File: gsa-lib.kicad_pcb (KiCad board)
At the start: 2 copper layers, 91 parts

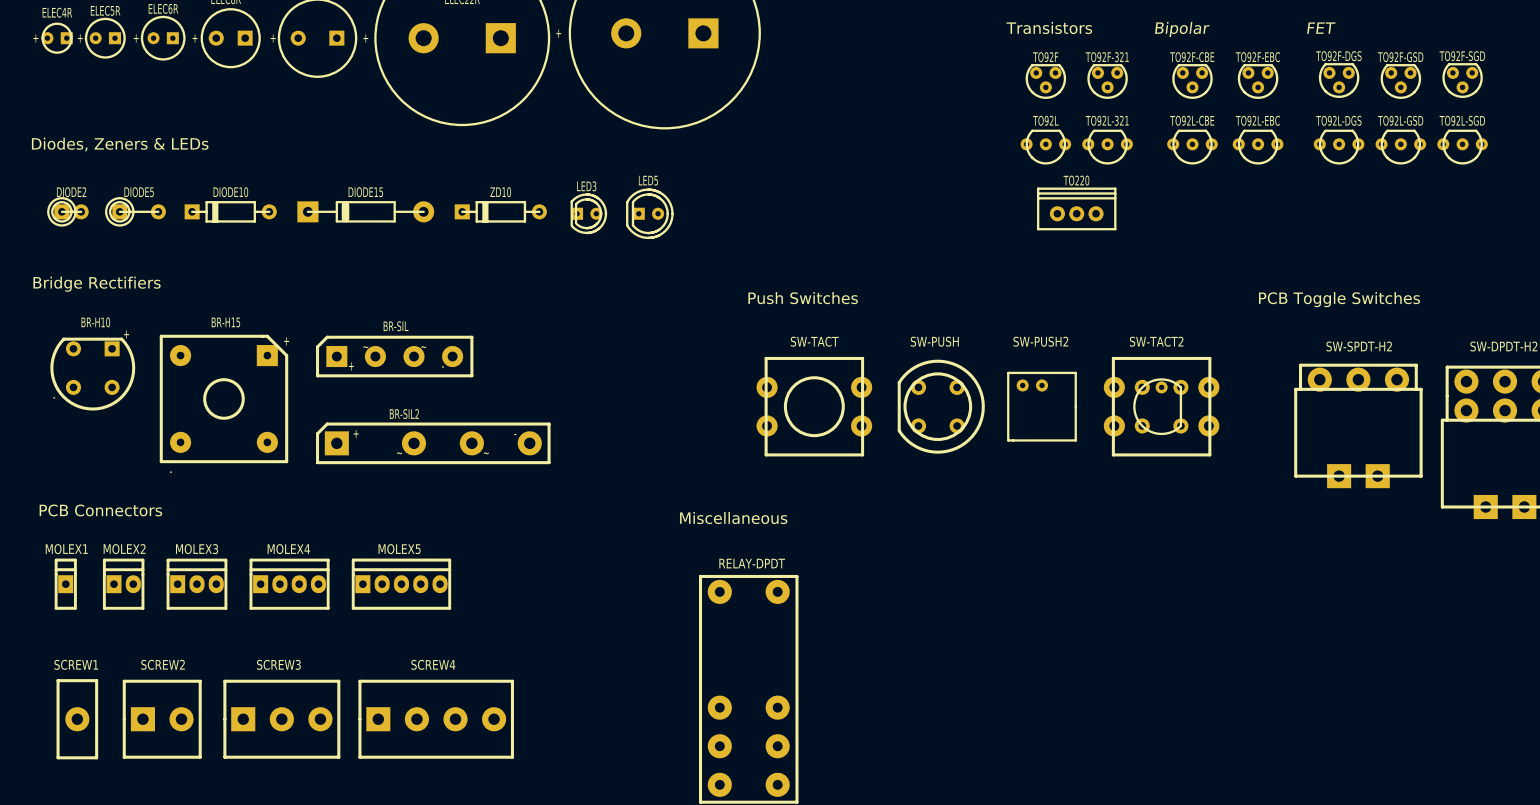
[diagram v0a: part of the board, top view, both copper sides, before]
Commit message: Add green LED variants to 3D models
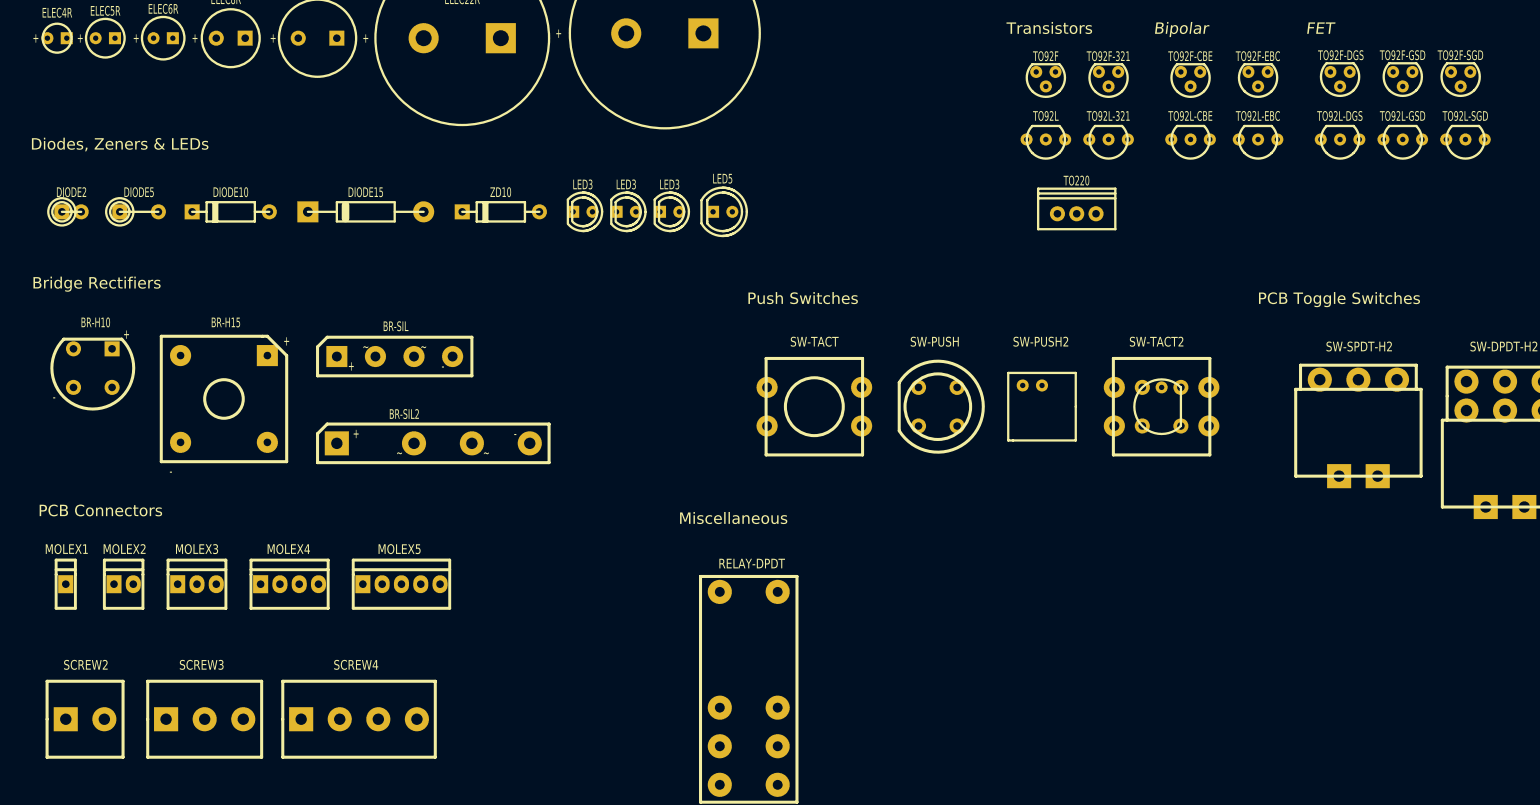
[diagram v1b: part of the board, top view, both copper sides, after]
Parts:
- removed SCREW1: 1term, gsa:SCREW1
- added LED3: 3mm, gsa:LED3, F.Cu at (102.9, 105.4)
- added LED3: 3mm, gsa:LED3, F.Cu at (97.2, 105.4)
- PAD-L: footprint gsa:PAD-XL -> gsa:PAD-L
- PAD-M: footprint gsa:PAD-L -> gsa:PAD-M
- PAD-S: footprint gsa:PAD-M -> gsa:PAD-S
- PAD-T: footprint gsa:PAD-S -> gsa:PAD-T
- PAD-XL: footprint gsa:PAD-XXL -> gsa:PAD-XL
- moved SCREW3 10.2 mm to (41.7, 172.2)
- moved SCREW2 10.2 mm to (25.9, 172.2)
- moved SCREW4 10.2 mm to (62.0, 172.2)
- moved LED5 9.78 mm to (109.9, 105.4)
- moved TO92L-SGD 0.74 mm to (207.6, 95.9)
- moved TO92L-CBE 0.68 mm to (171.4, 95.9)
- moved TO92L-GSD 0.68 mm to (199.4, 95.9)
- moved TO92L-321 0.65 mm to (160.7, 95.9)
- moved TO92L-DGS 0.65 mm to (191.1, 95.9)
- moved TO92L 0.63 mm to (152.4, 95.9)
- moved TO92L-EBC 0.63 mm to (180.3, 95.9)
- moved LED3 0.57 mm to (91.4, 105.4)
- moved TO92F-CBE 0.28 mm to (171.4, 88.3)
- moved TO92F-SGD 0.28 mm to (207.0, 88.3)
- moved TO92F-GSD 0.28 mm to (199.4, 88.3)
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
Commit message: Symbol and Footprint updates for GSA Emerald II
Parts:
- removed PAD-T: 0.7mm, gsa:PAD-T
- added LOGO-S: , gsa:LOGO-S, F.Cu at (140.5, 190.0)
- added LOGO_L: , gsa:LOGO-L, F.Cu at (125.5, 186.7)
- added LOGO_XS: , gsa:LOGO-XS, F.Cu at (140.5, 177.0)
- added PAD-XS: 0.7mm, gsa:PAD-XS, F.Cu at (19.1, 31.8)
- added POT-SNAP-H: , gsa:POT-SNAP-H, F.Cu at (245.1, 25.4)
- added POT-SNAP-V: , gsa:POT-SNAP-V, F.Cu at (260.4, 25.4)
- added POT-TRIM-H: , gsa:POT-TRIM-H, F.Cu at (245.1, 109.2)
- added SOIC8: 8pin SOIC, gsa:SOIC8, F.Cu at (180.3, 53.3)
- added SOT23-BCE: , gsa:SOT23-BCE, F.Cu at (171.4, 104.8)
- added SOT23-DGS: , gsa:SOT23-DGS, F.Cu at (191.1, 104.8)
- added TO92F-DSG: , gsa:TO92F-DSG, F.Cu at (215.3, 88.3)
- added TO92L-DSG: , gsa:TO92L-DSG, F.Cu at (215.9, 95.9)
- added TRIM-L: , gsa:TRIM-L, F.Cu at (238.8, 70.5)
- added TRIM-VS: , gsa:TRIM-VS, F.Cu at (238.8, 95.2)
- LED3: value 3mm -> 2mm
- moved TRIM-HS 40.4 mm to (238.8, 85.1)
- moved TRIM-V 24.0 mm to (238.8, 61.0)
- moved RELAY-DPDT 23.5 mm to (89.9, 153.4)
- moved TRIM-H 9.89 mm to (238.8, 48.3)
- moved POT-16 1.80 mm to (260.4, 70.4)
- moved POT-16-D 1.80 mm to (261.9, 90.7)
- moved POT-OMEG 1.80 mm to (256.3, 111.5)
- moved POT-DUAL 1.80 mm to (263.9, 152.7)
- moved POT-MIN 1.80 mm to (255.8, 39.4)
- moved POT-MIN-D 1.80 mm to (258.3, 53.1)
- moved POT-OMEG-D 1.80 mm to (263.9, 131.8)

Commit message: Overhaul and tidy-up of symbols, footprints and 3D models
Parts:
- removed 15pin TO220: TO220-15, gsa:TO220-15
- removed BR-SIL2: , gsa:BR-SIL2
- removed CAP-5-7: 5/7.5mm leads, gsa:CAP-5-7
- removed CAP-5-7-10: 5/7.5/10mm leads, gsa:CAP-5-7-10
- removed CAP1350: 13x5mm, gsa:CAP1350
- removed DIODE5: 5mm, gsa:DIODE5
- removed ELEC22R: 22mm, gsa:ELEC22R
- removed HOLE33: 3.3mm, gsa:HOLE33
- removed LOGO-S: , gsa:LOGO-S
- removed MOLEX5: 5pin, gsa:MOLEX5
- removed PAD-L: 1.5mm, gsa:PAD-L
- removed PAD-M: 1.3mm, gsa:PAD-M
- removed PAD-S: 1mm, gsa:PAD-S
- removed PAD-XL: 2.1mm, gsa:PAD-XL
- removed PAD-XS: 0.7mm, gsa:PAD-XS
- removed POT-DUAL: , gsa:POT-DUAL
- removed POT-TRIM-H: , gsa:POT-TRIM-H
- removed RELAY-DPDT: , gsa:RELAY-DPDT
- removed RES12: 12mm, gsa:RES12
- removed RES15: 15mm, gsa:RES15
- removed RES2: 2.5mm, gsa:RES2
- removed RES20: 20mm, gsa:RES20
- removed SCREW3: 3term, gsa:SCREW3
- removed SOT23-BCE: , gsa:SOT23-BCE
- removed SOT23-DGS: , gsa:SOT23-DGS
- removed SW-PUSH: , gsa:SW-PUSH
- removed SW-TACT2: , gsa:SW-TACT2
- removed TO92F-321: , gsa:TO92F-321
- removed TO92F-SGD: , gsa:TO92F-SGD
- removed TO92L-321: , gsa:TO92L-321
- removed TO92L-SGD: , gsa:TO92L-SGD
- removed ZD10: 10mm, gsa:ZENER10
- added 0.7mm: PAD07, gsa:PAD07, F.Cu at (19.1, 31.1)
- added 1.0mm: PAD10, gsa:PAD10, F.Cu at (24.8, 31.1)
- added 1.3mm: PAD13, gsa:PAD13, F.Cu at (31.1, 31.8)
- added 1.5mm: PAD15, gsa:PAD15, F.Cu at (37.5, 31.8)
- added 10mm: DIODE10, gsa:DIODE10, F.Cu at (44.5, 99.7)
- added 10x7mm: CAP1070, gsa:CAP1070, F.Cu at (104.1, 63.5)
- added 12.5mm: RES12, gsa:RES12, F.Cu at (66.0, 45.7)
- added 15mm: RES15, gsa:RES15, F.Cu at (83.8, 45.7)
- added 2.1mm: PAD21, gsa:PAD21, F.Cu at (44.5, 31.8)
- added 2.5mm: DIODE2, gsa:DIODE2, F.Cu at (23.5, 99.7)
- added 2.5mm: RES2, gsa:RES2, F.Cu at (19.7, 45.7)
- added 20mm: RES20, gsa:RES20, F.Cu at (105.4, 45.7)
- added 22mm: ELEC22R, gsa:ELEC22R, F.Cu at (75.6, 84.5)
- added 3.3mm: HOLE33-G, gsa:HOLE33-G, F.Cu at (59.7, 32.4)
- added 3.3mm: HOLE33, gsa:HOLE33, F.Cu at (51.4, 31.8)
- added 3term: SCREW3, gsa:SCREW3, F.Cu at (41.0, 174.8)
- added 5mm: DIODE5, gsa:DIODE5, F.Cu at (32.4, 99.7)
- added 5mm: RECT5, gsa:DIODE5, F.Cu at (33.0, 110.5)
- added 5pin: MOLEX5, gsa:MOLEX5, F.Cu at (66.9, 157.0)
- added 7.5/10mm: CAP-7-10, gsa:CAP-7-10, F.Cu at (116.8, 63.5)
- added 8mm: RES8, gsa:RES8, F.Cu at (38.1, 45.7)
- added ?: SOT23-DSG, gsa:SOT23-DSG, F.Cu at (199.4, 106.7)
- added ?: SOT23-GSD, gsa:SOT23-GSD, F.Cu at (209.6, 106.7)
- added ?: BR-SIL2, gsa:BR-SIL2, F.Cu at (68.0, 127.0)
- added ?: SW-PUSH1, gsa:SW-PUSH1, F.Cu at (191.1, 132.1)
- added ?: TO220-15, gsa:TO220-15, F.Cu at (179.1, 31.1)
- added ?: TO92L-ECB, gsa:TO92L-ECB, F.Cu at (188.0, 98.4)
- added ?: SW-DPDT-V2, gsa:SW-DPDT-V2, F.Cu at (168.3, 135.9)
- added ?: TO92F-ECB, gsa:TO92F-ECB, F.Cu at (188.0, 90.8)
- added ?: RELAY-DPDT, gsa:RELAY-DPDT, F.Cu at (88.3, 181.6)
- added ?: SOT23-BEC, gsa:SOT23-BEC, F.Cu at (167.6, 106.7)
- added ?: SOT23, gsa:SOT23, F.Cu at (153.0, 106.7)
- added ?: TO220-5, gsa:TO220-5, F.Cu at (198.8, 31.1)
- added ?: LOGO_S, gsa:LOGO-S, F.Cu at (140.3, 189.9)
- added ?: TO220-11, gsa:TO220-11, F.Cu at (156.2, 31.1)
- added Combined Pots: POT-DUAL, gsa:POT-DUAL, F.Cu at (265.4, 158.1)
- added Combined Push Switches: SW-TACT-ALL, gsa:SW-TACT-ALL, F.Cu at (210.2, 149.2)
- added Reversible Pot/Trimmer: POT-TRIM-HR, gsa:POT-TRIM-HR, F.Cu at (247.0, 115.6)
- 10mm: renamed from ELEC10R; value 10mm -> ELEC10R
- 10mm: renamed from DIODE10; value 10mm -> RECT10
- 10mm: renamed from RES10; value 10mm -> RES10
- 10x3.5mm: renamed from CAP1035; value 10x3.5mm -> CAP1035
- 14pin DIL: renamed from DIL14; value 14pin DIL -> DIL14
- 15mm: renamed from DIODE15; value 15mm -> RECT15
- 16pin DIL: renamed from DIL16; value 16pin DIL -> DIL16
- 1pin: renamed from MOLEX1; value 1pin -> MOLEX1
- 2.5mm: renamed from DIODE2; value 2.5mm -> RECT2
- 2.5mm: renamed from LINK2; value 2.5mm -> LINK2
- 2.5mm: renamed from CAP-C25; value 2.5mm -> CAP-C25
- 25mm: renamed from ELEC25R; value 25mm -> ELEC25R
- 2mm: renamed from LED3; value 2mm -> LED3
- 2pin: renamed from MOLEX2; value 2pin -> MOLEX2
- 2term: renamed from SCREW2; value 2term -> SCREW2
- 3mm (x2): renamed from LED3; value 3mm -> LED3
- 3pin: renamed from MOLEX3; value 3pin -> MOLEX3
- 4mm: renamed from ELEC4R; value 4mm -> ELEC4R
- 4pin: renamed from MOLEX4; value 4pin -> MOLEX4
- 4term: renamed from SCREW4; value 4term -> SCREW4
- 5mm: renamed from ELEC5R; value 5mm -> ELEC5R
- 5mm: renamed from LED5; value 5mm -> LED5
- 5mm: renamed from LINK5; value 5mm -> LINK5
- 5mm: renamed from RES5; value 5mm -> RES5
- 5mm: renamed from CAP-C50; value 5mm -> CAP-C50
- 6mm: renamed from ELEC6R; value 6mm -> ELEC6R
- 7.5x2.5mm: renamed from CAP725; value 7.5x2.5mm -> CAP725
- 7.5x3.5mm: renamed from CAP735; value 7.5x3.5mm -> CAP735
- 7.5x3mm: renamed from CAP730; value 7.5x3mm -> CAP730
- 7.5x4mm: renamed from CAP740; value 7.5x4mm -> CAP740
- 7.5x5mm: renamed from CAP750; value 7.5x5mm -> CAP750
- 78xx Regulator: renamed from REG78; value 78xx Regulator -> REG78
- 79xx Regulator: renamed from REG79; value 79xx Regulator -> REG79
- 8mm: renamed from ELEC8R; value 8mm -> ELEC8R
- 8pin: renamed from SOIC8; value 8pin SOIC -> SOIC8
- 8pin DIL: renamed from DIL8; value 8pin DIL -> DIL8
- ?: renamed from TO92L-DSG; value (none) -> TO92L-DSG
- ?: renamed from TO92L-GSD; value (none) -> TO92L-GSD
- ?: renamed from TO92L-DGS; value (none) -> TO92L-DGS
- ?: renamed from TO92L-EBC; value (none) -> TO92L-EBC
- ?: renamed from TO92L-CBE; value (none) -> TO92L-CBE
- ?: renamed from TO92L; value (none) -> TO92L
- ?: renamed from TO92F-DSG; value (none) -> TO92F-DSG
- ?: renamed from TO92F-DGS; value (none) -> TO92F-DGS
- ?: renamed from TO92F-EBC; value (none) -> TO92F-EBC
- ?: renamed from TO92F-CBE; value (none) -> TO92F-CBE
- ?: renamed from TO92F; value (none) -> TO92F
- ?: renamed from TO92F-GSD; value (none) -> TO92F-GSD
- ?: renamed from SW-PUSH2; value (none) -> SW-PUSH2
- ?: renamed from POT-SNAP-V; value (none) -> POT-SNAP-V
- ?: renamed from POT-SNAP-H; value (none) -> POT-SNAP-H
- ?: renamed from SW-SPDT-V2; value (none) -> SW-SPDT-V2
- ?: renamed from LOGO_XS; value (none) -> LOGO_XS
- ?: renamed from LOGO_L; value (none) -> LOGO_L
- ?: renamed from TRIM-L; value (none) -> TRIM-L
- ?: renamed from TRIM-VS; value (none) -> TRIM-VS
- ?: renamed from TRIM-HS; value (none) -> TRIM-HS
- ?: renamed from TRIM-V; value (none) -> TRIM-V
- ?: renamed from TRIM-H; value (none) -> TRIM-H
- ?: renamed from POT-OMEG-D; value (none) -> POT-OMEG-D
- ?: renamed from POT-OMEG; value (none) -> POT-OMEG
- ?: renamed from POT-16-D; value (none) -> POT-16-D
- ?: renamed from POT-16; value (none) -> POT-16
- ?: renamed from POT-MIN-D; value (none) -> POT-MIN-D
- ?: renamed from POT-MIN; value (none) -> POT-MIN
- ?: renamed from SW-DPDT-H2; value (none) -> SW-DPDT-H2
- ?: renamed from SW-SPDT-H2; value (none) -> SW-SPDT-H2
- ?: renamed from SW-TACT; value (none) -> SW-TACT
- ?: renamed from TO220; value (none) -> TO220
- moved ? 75.1 mm to (155.6, 135.9), turned to 0 degrees
- moved ? 74.0 mm to (120.7, 127.6), turned to 0 degrees
- moved ? 73.6 mm to (140.3, 131.4), turned to 0 degrees
- moved ? 71.6 mm to (191.1, 149.2)
- moved ? 58.3 mm to (210.2, 132.1), turned to 0 degrees
- moved 8pin 29.0 mm to (208.3, 61.0)
- moved ? 24.6 mm to (153.0, 81.3)
- moved 14pin DIL 23.7 mm to (170.8, 61.0)
- moved 16pin DIL 23.7 mm to (192.8, 61.0)
- moved 8pin DIL 23.7 mm to (153.4, 61.0)
- moved 78xx Regulator 21.2 mm to (167.0, 46.6)
- moved 79xx Regulator 21.2 mm to (153.3, 46.6)
- moved 2mm 13.1 mm to (79.4, 110.5)
- moved ? 12.8 mm to (64.0, 137.0)
- moved 3mm 12.5 mm to (85.7, 110.5)
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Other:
- board text added: "Disc"
- board text added: "Film"
- board text added: "Logos"
- board text added: "SMT"

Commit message: Updates for KiCad v9
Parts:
- added 1.1mm: PAD11, GSA:PAD11, F.Cu at (30.5, 31.2)
- added 10mm: LINK10, GSA:LINK10, F.Cu at (94.8, 32.2)
- added REF**: TO92L-BEB, GSA:TO92L-BEB, F.Cu at (216.0, 100.0)
- added REF**: TO92F-BEB, GSA:TO92F-BEB, F.Cu at (216.0, 92.5)
- added REF**: RELAY-S-DPDT, GSA:RELAY-S-DPDT, F.Cu at (97.5, 163.0)
- 0.7mm: footprint gsa:PAD07 -> GSA:PAD07
- 1.0mm: footprint gsa:PAD10 -> GSA:PAD10
- 1.3mm: footprint gsa:PAD13 -> GSA:PAD13
- 1.5mm: footprint gsa:PAD15 -> GSA:PAD15
- 10mm: footprint gsa:RES10 -> GSA:RES10
- 10mm: footprint gsa:ELEC10R -> GSA:ELEC10R
- 10mm (x2): footprint gsa:DIODE10 -> GSA:DIODE10
- 10x3.5mm: footprint gsa:CAP1035 -> GSA:CAP1035
- 10x7mm: footprint gsa:CAP1070 -> GSA:CAP1070
- 12.5mm: footprint gsa:RES12 -> GSA:RES12
- 14pin DIL: footprint gsa:DIL14 -> GSA:DIL14
- 15mm: footprint gsa:DIODE15 -> GSA:DIODE15
- 15mm: footprint gsa:RES15 -> GSA:RES15
- 16pin DIL: footprint gsa:DIL16 -> GSA:DIL16
- 1pin: footprint gsa:MOLEX1 -> GSA:MOLEX1
- 2.1mm: footprint gsa:PAD21 -> GSA:PAD21
- 2.5mm: footprint gsa:CAP-C25 -> GSA:CAP-C25
- 2.5mm: footprint gsa:LINK2 -> GSA:LINK2
- 2.5mm (x2): footprint gsa:DIODE2 -> GSA:DIODE2
- 2.5mm: footprint gsa:RES2 -> GSA:RES2
- 20mm: footprint gsa:RES20 -> GSA:RES20
- 22mm: footprint gsa:ELEC22R -> GSA:ELEC22R
- 25mm: footprint gsa:ELEC25R -> GSA:ELEC25R
- 2mm, 3mm (x2): footprint gsa:LED3 -> GSA:LED3
- 2pin: footprint gsa:MOLEX2 -> GSA:MOLEX2
- 2term: footprint gsa:SCREW2 -> GSA:SCREW2
- 3.3mm: footprint gsa:HOLE33 -> GSA:HOLE33
- 3.3mm: footprint gsa:HOLE33-G -> GSA:HOLE33-G
- 3pin: footprint gsa:MOLEX3 -> GSA:MOLEX3
- 3term: footprint gsa:SCREW3 -> GSA:SCREW3
- 4mm: footprint gsa:ELEC4R -> GSA:ELEC4R
- 4pin: footprint gsa:MOLEX4 -> GSA:MOLEX4
- 4term: footprint gsa:SCREW4 -> GSA:SCREW4
- 5mm: footprint gsa:RES5 -> GSA:RES5
- 5mm: footprint gsa:LINK5 -> GSA:LINK5
- 5mm: footprint gsa:ELEC5R -> GSA:ELEC5R
- 5mm: footprint gsa:LED5 -> GSA:LED5
- 5mm: footprint gsa:CAP-C50 -> GSA:CAP-C50
- 5mm (x2): footprint gsa:DIODE5 -> GSA:DIODE5
- 5pin: footprint gsa:MOLEX5 -> GSA:MOLEX5
- 6mm: footprint gsa:ELEC6R -> GSA:ELEC6R
- 7.5/10mm: footprint gsa:CAP-7-10 -> GSA:CAP-7-10
- 7.5x2.5mm: footprint gsa:CAP725 -> GSA:CAP725
- 7.5x3.5mm: footprint gsa:CAP735 -> GSA:CAP735
- 7.5x3mm: footprint gsa:CAP730 -> GSA:CAP730
- 7.5x4mm: footprint gsa:CAP740 -> GSA:CAP740
- 7.5x5mm: footprint gsa:CAP750 -> GSA:CAP750
- 78xx Regulator: footprint gsa:REG78 -> GSA:REG78
- 79xx Regulator: footprint gsa:REG79 -> GSA:REG79
- 8mm: footprint gsa:ELEC8R -> GSA:ELEC8R
- 8mm: footprint gsa:RES8 -> GSA:RES8
- 8pin: footprint gsa:SOIC8 -> GSA:SOIC8
- 8pin DIL: footprint gsa:DIL8 -> GSA:DIL8
- ?: footprint gsa:SW-DPDT-H2 -> GSA:SW-DPDT-H2
- ?: footprint gsa:TO92F-DGS -> GSA:TO92F-DGS
- ?: footprint gsa:TO92F-GSD -> GSA:TO92F-GSD
- ?: footprint gsa:TO92L-DGS -> GSA:TO92L-DGS
- ?: footprint gsa:TO92L-GSD -> GSA:TO92L-GSD
- ?: footprint gsa:TO220 -> GSA:TO220
- ?: footprint gsa:POT-MIN -> GSA:POT-MIN
- ?: footprint gsa:POT-MIN-D -> GSA:POT-MIN-D
- ?: footprint gsa:POT-16 -> GSA:POT-16
- ?: footprint gsa:POT-16-D -> GSA:POT-16-D
- ?: footprint gsa:POT-OMEG -> GSA:POT-OMEG
- ?: footprint gsa:SW-SPDT-H2 -> GSA:SW-SPDT-H2
- ?: footprint gsa:POT-OMEG-D -> GSA:POT-OMEG-D
- ?: footprint gsa:SW-TACT -> GSA:SW-TACT
- ?: footprint gsa:SW-PUSH2 -> GSA:SW-PUSH2
- ?: footprint gsa:TO92F-DSG -> GSA:TO92F-DSG
- ?: footprint gsa:TO92L-DSG -> GSA:TO92L-DSG
- ?: footprint gsa:TRIM-H -> GSA:TRIM-H
- ?: footprint gsa:TRIM-V -> GSA:TRIM-V
- ?: footprint gsa:TRIM-VS -> GSA:TRIM-VS
- ?: footprint gsa:TRIM-HS -> GSA:TRIM-HS
- ?: footprint gsa:TRIM-L -> GSA:TRIM-L
- ?: footprint gsa:SW-SPDT-V2 -> GSA:SW-SPDT-V2
- ?: footprint gsa:LOGO-L -> GSA:LOGO-L
- ?: footprint gsa:LOGO-XS -> GSA:LOGO-XS
- ?: footprint gsa:POT-SNAP-V -> GSA:POT-SNAP-V
- ?: footprint gsa:POT-SNAP-H -> GSA:POT-SNAP-H
- ?: footprint gsa:SW-PUSH1 -> GSA:SW-PUSH1
- ?: footprint gsa:SW-DPDT-V2 -> GSA:SW-DPDT-V2
- ?: footprint gsa:BR-H10 -> GSA:BR-H10
- ?: footprint gsa:BR-H15 -> GSA:BR-H15
- ?: footprint gsa:BR-SIL -> GSA:BR-SIL
- ?: footprint gsa:BR-SIL2 -> GSA:BR-SIL2
- ?: footprint gsa:TO92F -> GSA:TO92F
- ?: footprint gsa:TO220-15 -> GSA:TO220-15
- ?: footprint gsa:RELAY-DPDT -> GSA:RELAY-DPDT
- ?: footprint gsa:TO220-11 -> GSA:TO220-11
- ?: footprint gsa:LOGO-S -> GSA:LOGO-S
- ?: footprint gsa:TO220-5 -> GSA:TO220-5
- ?: footprint gsa:TO92F-ECB -> GSA:TO92F-ECB
- ?: footprint gsa:TO92L-ECB -> GSA:TO92L-ECB
- ?: footprint gsa:SOT23-GSD -> GSA:SOT23-GSD
- ?: footprint gsa:SOT23 -> GSA:SOT23
- ?: footprint gsa:SOT23-DSG -> GSA:SOT23-DSG
- ?: footprint gsa:TO92F-CBE -> GSA:TO92F-CBE
- ?: footprint gsa:SOT23-BEC -> GSA:SOT23-BEC
- ?: footprint gsa:TO92F-EBC -> GSA:TO92F-EBC
- ?: footprint gsa:TO92L -> GSA:TO92L
- ?: footprint gsa:TO92L-CBE -> GSA:TO92L-CBE
- ?: footprint gsa:TO92L-EBC -> GSA:TO92L-EBC
- Combined Pots: footprint gsa:POT-DUAL -> GSA:POT-DUAL
- Combined Push Switches: footprint gsa:SW-TACT-ALL -> GSA:SW-TACT-ALL
- Reversible Pot/Trimmer: footprint gsa:POT-TRIM-HR -> GSA:POT-TRIM-HR
- moved ? 13.9 mm to (195.8, 92.4)
- moved ? 13.9 mm to (195.8, 100.0)
- moved ? 13.9 mm to (205.9, 92.4)
- moved ? 13.9 mm to (205.9, 100.0)
- moved ? 13.9 mm to (174.2, 92.4)
- moved ? 13.9 mm to (174.2, 100.0)
- moved ? 13.9 mm to (195.8, 108.3)
- moved ? 13.9 mm to (164.0, 92.4)
- moved ? 13.9 mm to (164.0, 100.0)
- moved ? 13.9 mm to (185.6, 92.4)
- moved ? 13.9 mm to (185.6, 100.0)
- moved ? 13.9 mm to (185.6, 108.3)
- moved ? 13.9 mm to (153.8, 92.4)
- moved ? 13.9 mm to (153.8, 108.3)
- moved ? 13.9 mm to (153.8, 100.0)
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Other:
- net class Default removed
- board text added: "UJT"
